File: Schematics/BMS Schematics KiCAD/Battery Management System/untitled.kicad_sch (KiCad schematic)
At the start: 29 parts, among them Q23 2N7002, Q24 2N7002, Q25 2N7002, Q26 2N7002, Q27 IRF9540NSTRLPBF, Q28 IRF9540NSTRLPBF, Q29 IRF9540NSTRLPBF, Q30 IRF9540NSTRLPBF, Q31 IRF9540NSTRLPBF, Q32 2N7002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

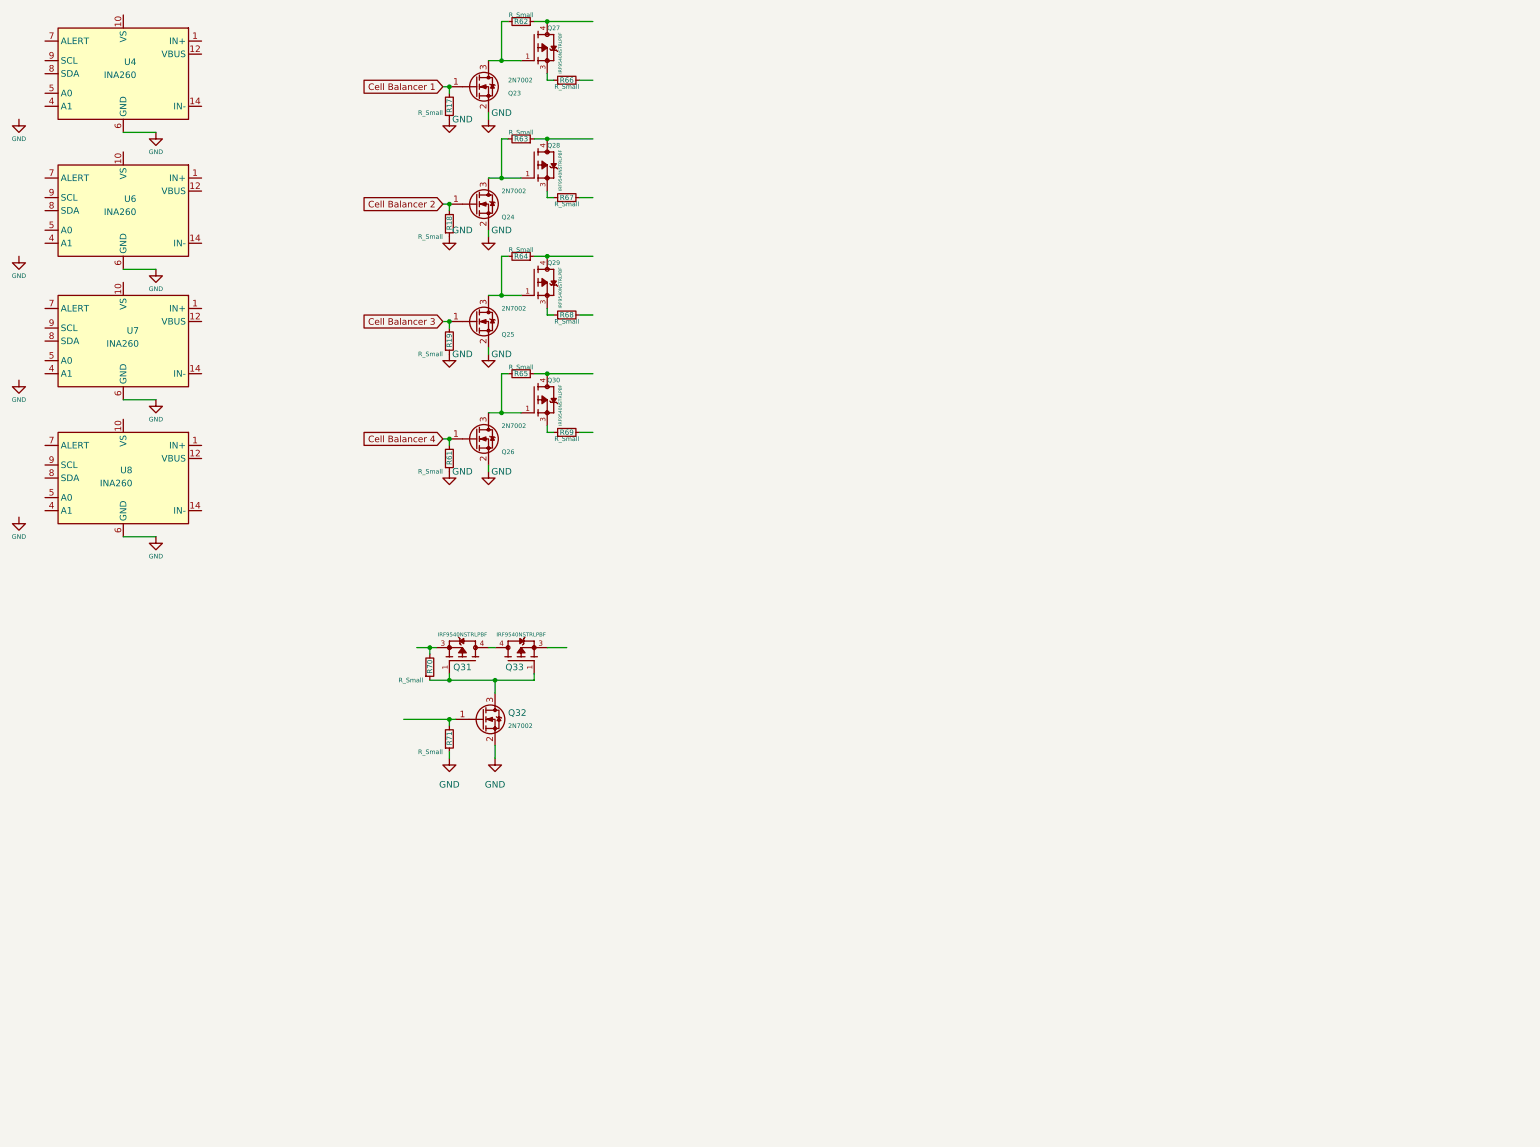
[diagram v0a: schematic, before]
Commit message: Pulled together root sheet so that it's obvious how the power flows and how the blocks are connected. Finally, a decent block diagram :)
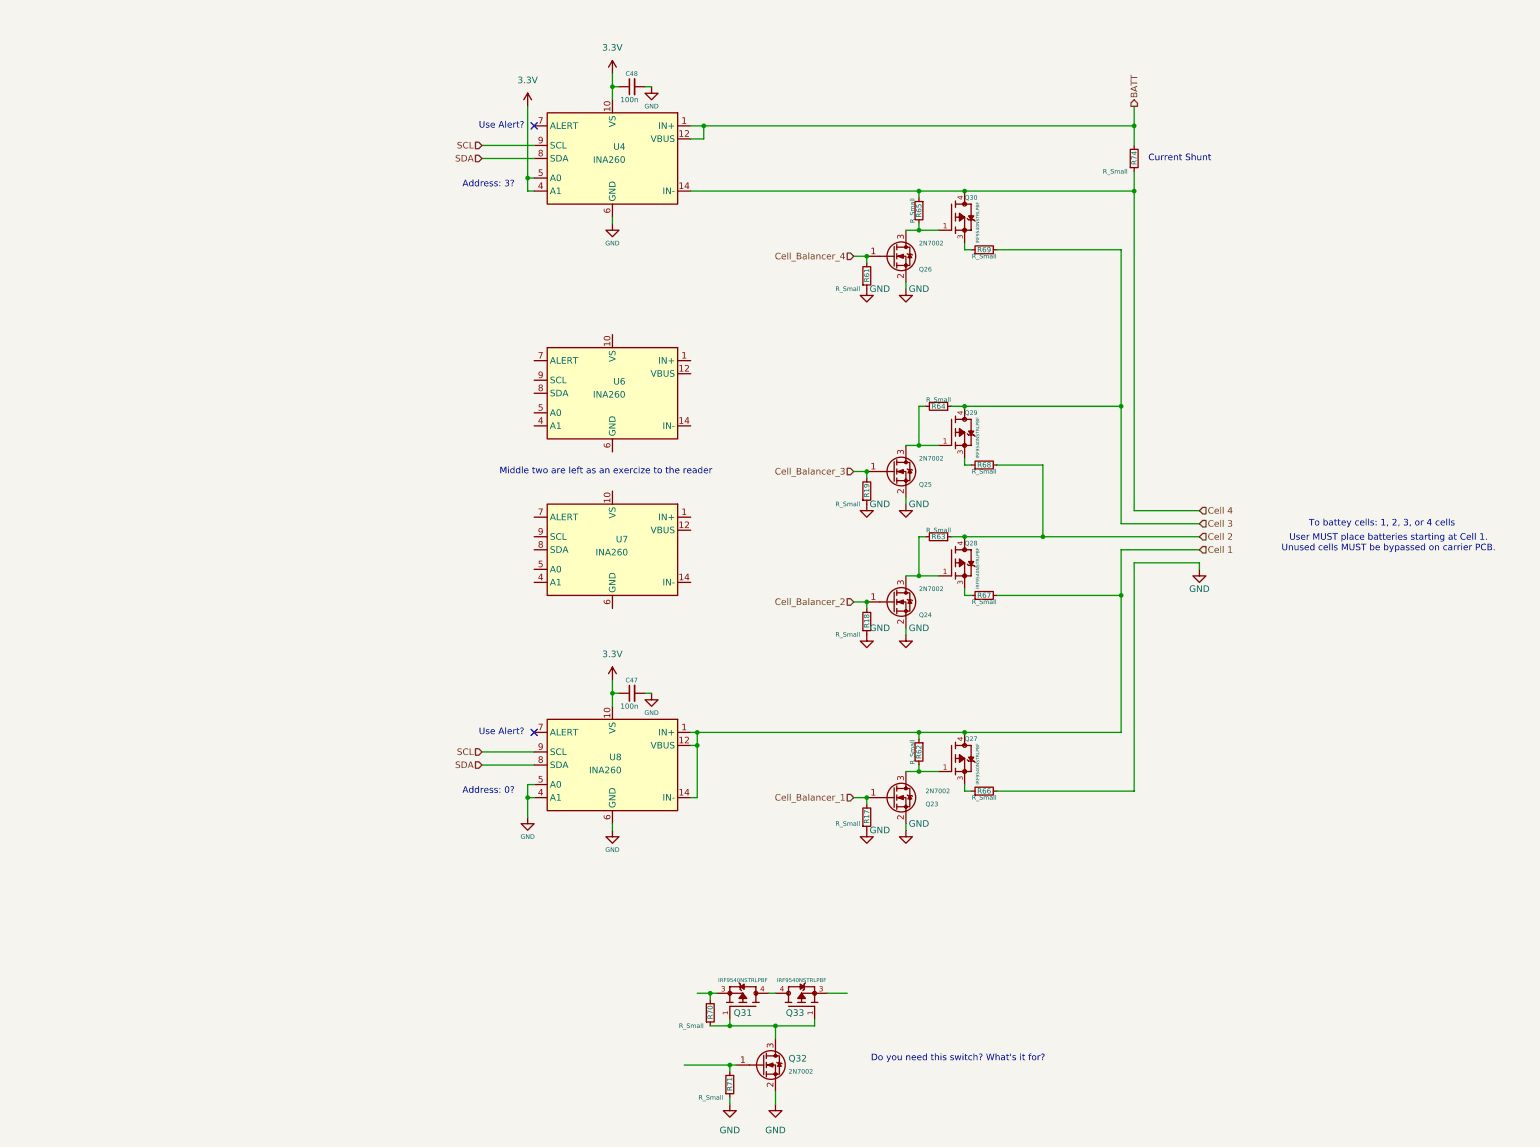
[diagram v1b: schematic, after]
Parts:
- added C47, C48: 100n, Capacitor_SMD:C_0201_0603Metric, symbol Device:C_Small
- added R74: R_Small, Resistor_SMD:R_0201_0603Metric, symbol Device:R_Small
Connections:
- net GND: now also R66.2, U8.4 (A1), U8.5 (A0), C47.2, C48.2; no longer U6.6 (GND), U7.6 (GND)
- net Cell 3: now reaches Q29.4, R64.1
- net Cell 3: now also R69.2
- net Cell 1: now reaches Q27.4, R62.1
- net Cell 1: now also R67.2, U8.1 (IN+), U8.12 (VBUS), U8.14 (IN-)
- net Cell 4: now reaches Q30.4, R65.1
- net Cell 4: now also U4.14 (IN-), R74.1
- net BATT: now reaches U4.1 (IN+)
- net BATT: now also U4.12 (VBUS), R74.2
- net 3.3V: now reaches U4.10 (VS)
- net 3.3V: now also U4.4 (A1), U4.5 (A0), U8.10 (VS), C47.1, C48.1
- net SDA: now reaches U4.8 (SDA)
- net SDA: now also U8.8 (SDA)
- net SCL: now reaches U4.9 (SCL)
- net SCL: now also U8.9 (SCL)
- net Cell 2: now reaches R68.2
- net Cell 2: now also Q28.4, R63.1
- net Cell Balancer 1 renamed Cell_Balancer_1
- net Cell Balancer 2 renamed Cell_Balancer_2
- net Cell Balancer 3 renamed Cell_Balancer_3
- net Cell Balancer 4 renamed Cell_Balancer_4
- no-connect marks 0 -> 2
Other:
- note added: "Address: 0?"
- note added: "Address: 3?"
- note added: "Current Shunt"
- note added: "Do you need this switch? What's it for?"
- note added: "Middle two are left as an exercize to the reader"
- note added: "To battey cells: 1, 2, 3, or 4 cells"
- note added: "Use Alert?"
- note added: "User MUST place batteries starting at Cell 1. Unused cells MUST be bypassed on carrier PCB."
- moved on the sheet: Q23, Q24, Q25, Q26, Q27, Q28, Q29, Q30, Q31, Q32, Q33, R17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
